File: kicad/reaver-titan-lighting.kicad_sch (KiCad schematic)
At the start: 23 parts, among them J1 T-Connector Deans 14 AWG, Q1 IRLML6344, Q2 IRLML6344, Q3 IRLML6344, Q4 IRLML6344, Q5 IRLML6344, SW1 Latching Push Button, U1 JZK 2S 7.4V 8A BMS, U2 MP1584 Buck Converter 5V, U3 ESP32-S3 Super Mini, U4 PCA9685PW

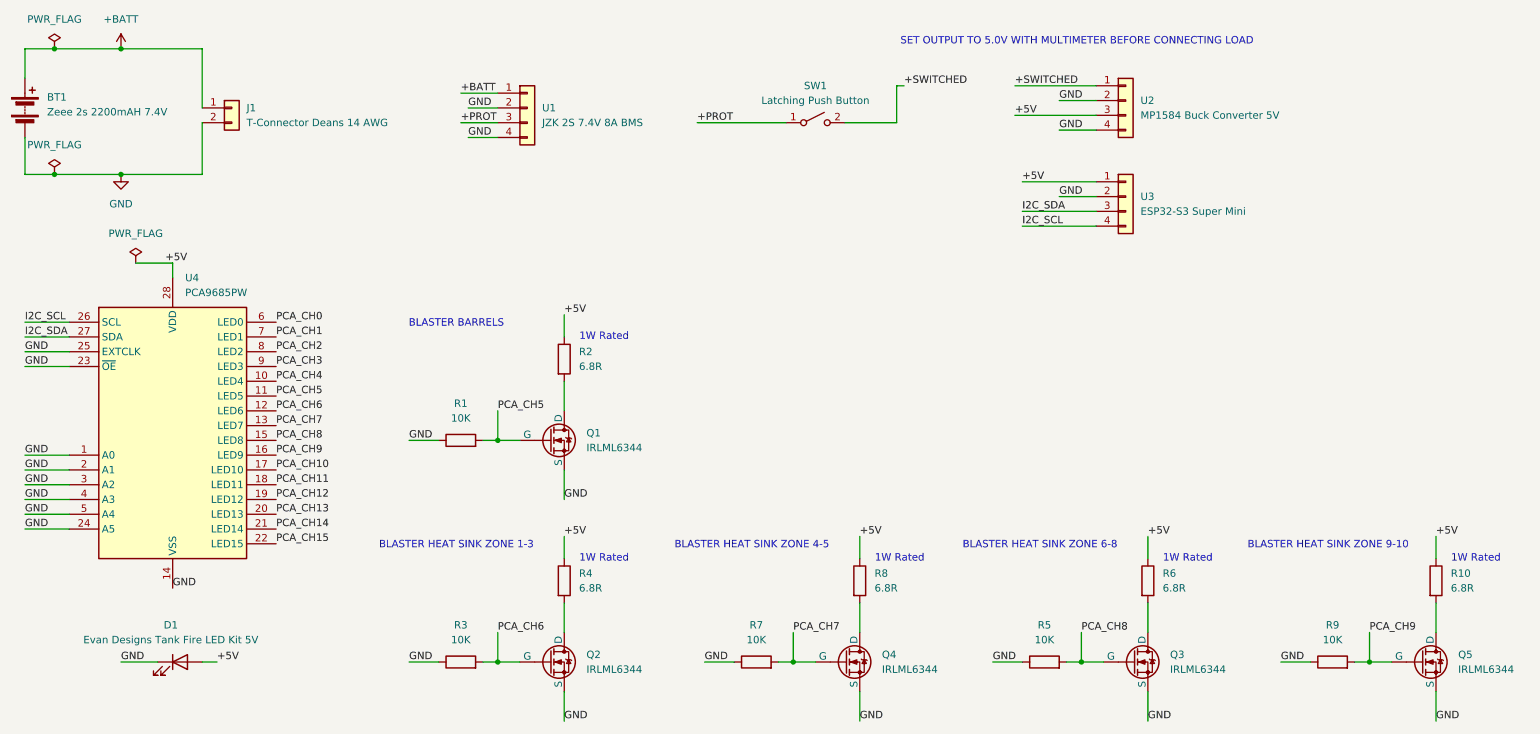
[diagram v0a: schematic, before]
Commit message: feat: separate schematic into hierarchical sheets (#25)
Split the flat reaver-titan-lighting.kicad_sch into a root navigation
sheet with two hierarchical sub-sheets: core-power.kicad_sch and
blaster-zones.kicad_sch. Cross-sheet PCA9685 channel signals use global
labels (PCA_CH5–9). Consolidated versioned ERC reports into single ERC.rpt.

Closes #22

Co-authored-by: Claude Sonnet 4.6 <noreply@anthropic.com>
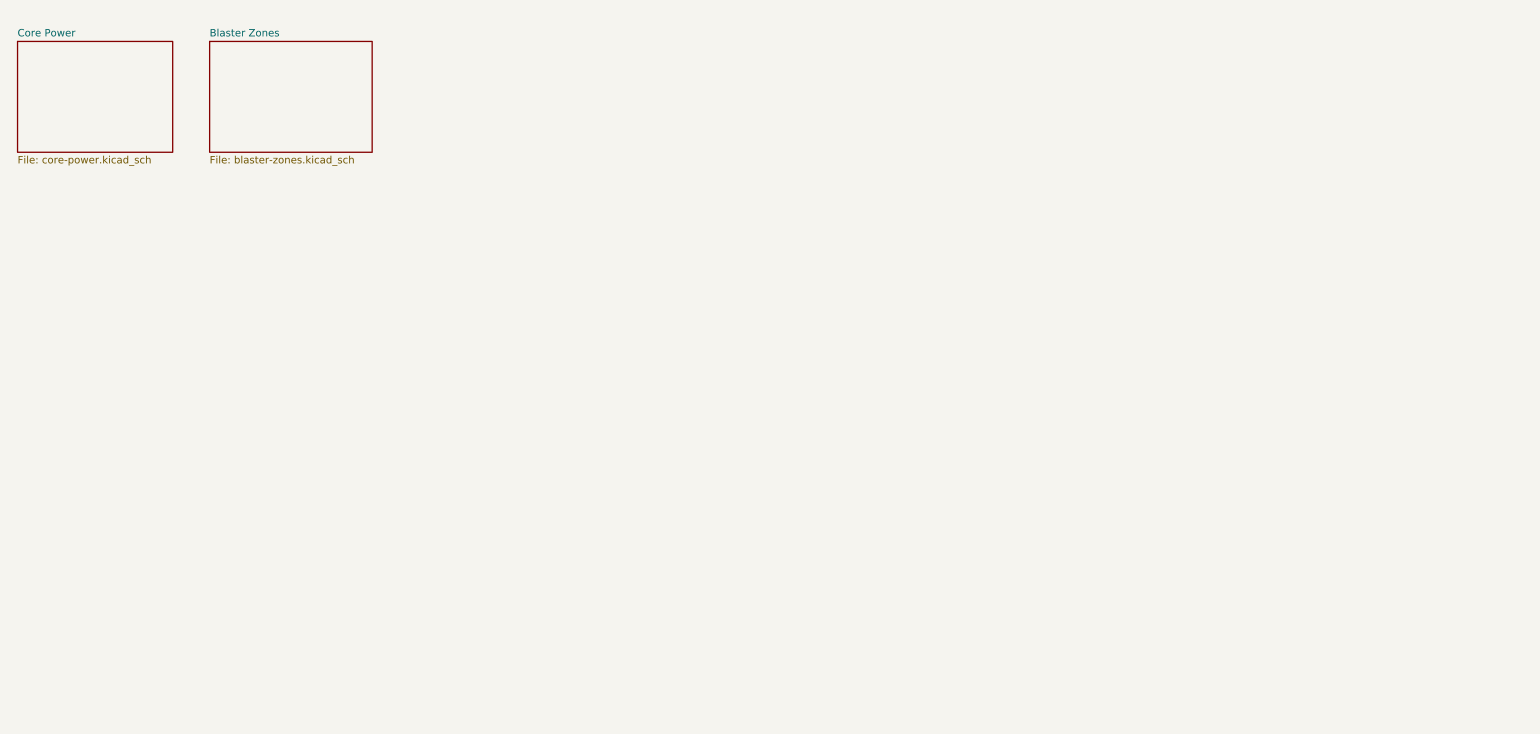
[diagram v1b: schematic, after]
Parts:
- removed BT1: Zeee 2s 2200mAH 7.4V, symbol Device:Battery
- removed D1: Evan Designs Tank Fire LED Kit 5V, symbol Device:LED
- removed J1: T-Connector Deans 14 AWG, symbol Connector_Generic:Conn_01x02
- removed Q1, Q2, Q3, Q4, Q5: IRLML6344, symbol Simulation_SPICE:NMOS
- removed R1, R3, R5, R7, R9: 10K, symbol Device:R
- removed R10, R2, R4, R6, R8: 6.8R, symbol Device:R
- removed SW1: Latching Push Button, symbol Switch:SW_SPST
- removed U1: JZK 2S 7.4V 8A BMS, symbol Connector_Generic:Conn_01x04
- removed U2: MP1584 Buck Converter 5V, symbol Connector_Generic:Conn_01x04
- removed U3: ESP32-S3 Super Mini, symbol Connector_Generic:Conn_01x04
- removed U4: PCA9685PW, Package_SO:TSSOP-28_4.4x9.7mm_P0.65mm, symbol Driver_LED:PCA9685PW
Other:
- added sheet Blaster Zones (blaster-zones.kicad_sch)
- added sheet Core Power (core-power.kicad_sch)
- note removed: "1W Rated"
- note removed: "BLASTER BARRELS"
- note removed: "BLASTER HEAT SINK ZONE 1-3"
- note removed: "BLASTER HEAT SINK ZONE 4-5"
- note removed: "BLASTER HEAT SINK ZONE 6-8"
- note removed: "BLASTER HEAT SINK ZONE 9-10"
- note removed: "SET OUTPUT TO 5.0V WITH MULTIMETER BEFORE CONNECTING LOAD"

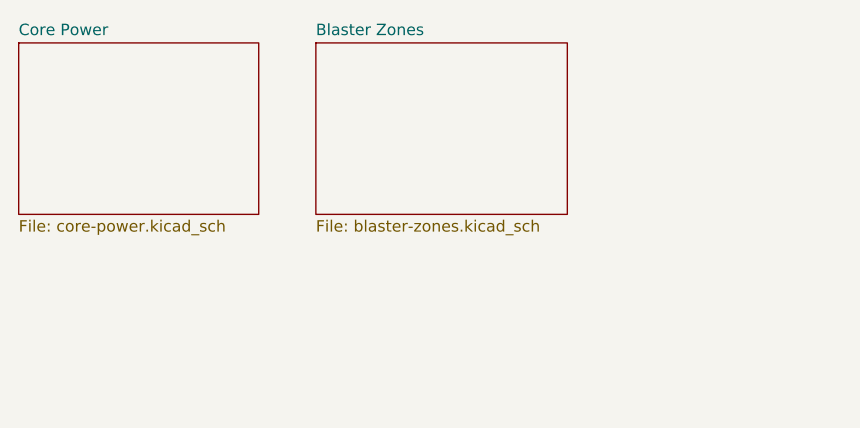
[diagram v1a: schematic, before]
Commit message: docs: rename schematic sheets and add SVG exports
- Rename core-power.kicad_sch → core-infrastructure.kicad_sch
- Rename blaster-zones.kicad_sch → blaster.kicad_sch
- Export core-infrastructure.svg and blaster.svg from KiCad
- Update SVG references in core-infrastructure.md and blaster.md
- Update CLAUDE.md schematic table to reflect new filenames

Closes #21

Co-Authored-By: Claude Sonnet 4.6 <noreply@anthropic.com>
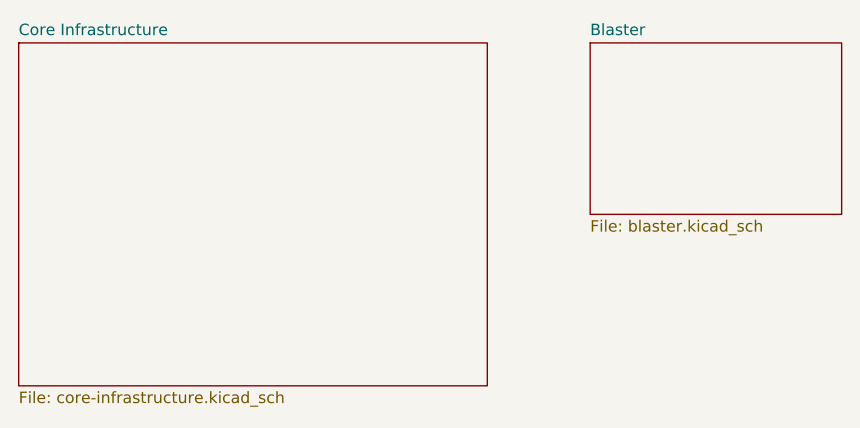
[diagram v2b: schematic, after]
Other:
- sheet Blaster Zones renamed Blaster
- sheet Core Power renamed Core Infrastructure
- sheet Blaster: file blaster-zones.kicad_sch -> blaster.kicad_sch
- sheet Core Infrastructure: file core-power.kicad_sch -> core-infrastructure.kicad_sch
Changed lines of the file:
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@@
 	(sheet
 		(at 25.4 25.4)
-		(size 26.67 19.05)
+		(size 52.07 38.1)
 		(exclude_from_sim no)
 		(in_bom yes)
@@
 			(color 0 0 0 0)
 		)
-		(property "Sheetname" "Core Power"
+		(property "Sheetname" "Core Infrastructure"
 			(at 25.4 24.6884 0)
 			(show_name no)
@@
 			)
 		)
-		(property "Sheetfile" "core-power.kicad_sch"
-			(at 25.4 45.0346 0)
+		(property "Sheetfile" "core-infrastructure.kicad_sch"
+			(at 25.4 64.0846 0)
 			(show_name no)
 			(do_not_autoplace no)
@@
 	)
 	(sheet
-		(at 58.42 25.4)
+		(at 88.9 25.4)
 		(size 27.94 19.05)
 		(exclude_from_sim no)
@@
 			(color 0 0 0 0)
 		)
-		(property "Sheetname" "Blaster Zones"
-			(at 58.42 24.6884 0)
+		(property "Sheetname" "Blaster"
+			(at 88.9 24.6884 0)
 			(show_name no)
 			(do_not_autoplace no)
@@
 			)
 		)
-		(property "Sheetfile" "blaster-zones.kicad_sch"
-			(at 58.42 45.0346 0)
+		(property "Sheetfile" "blaster.kicad_sch"
+			(at 88.9 45.0346 0)
 			(show_name no)
 			(do_not_autoplace no)
